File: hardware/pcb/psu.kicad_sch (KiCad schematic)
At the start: 24 parts, among them P1 2S LiPo Connector, Q3 AO3401A, SW1 SW_SPDT, U1 AP63203WU

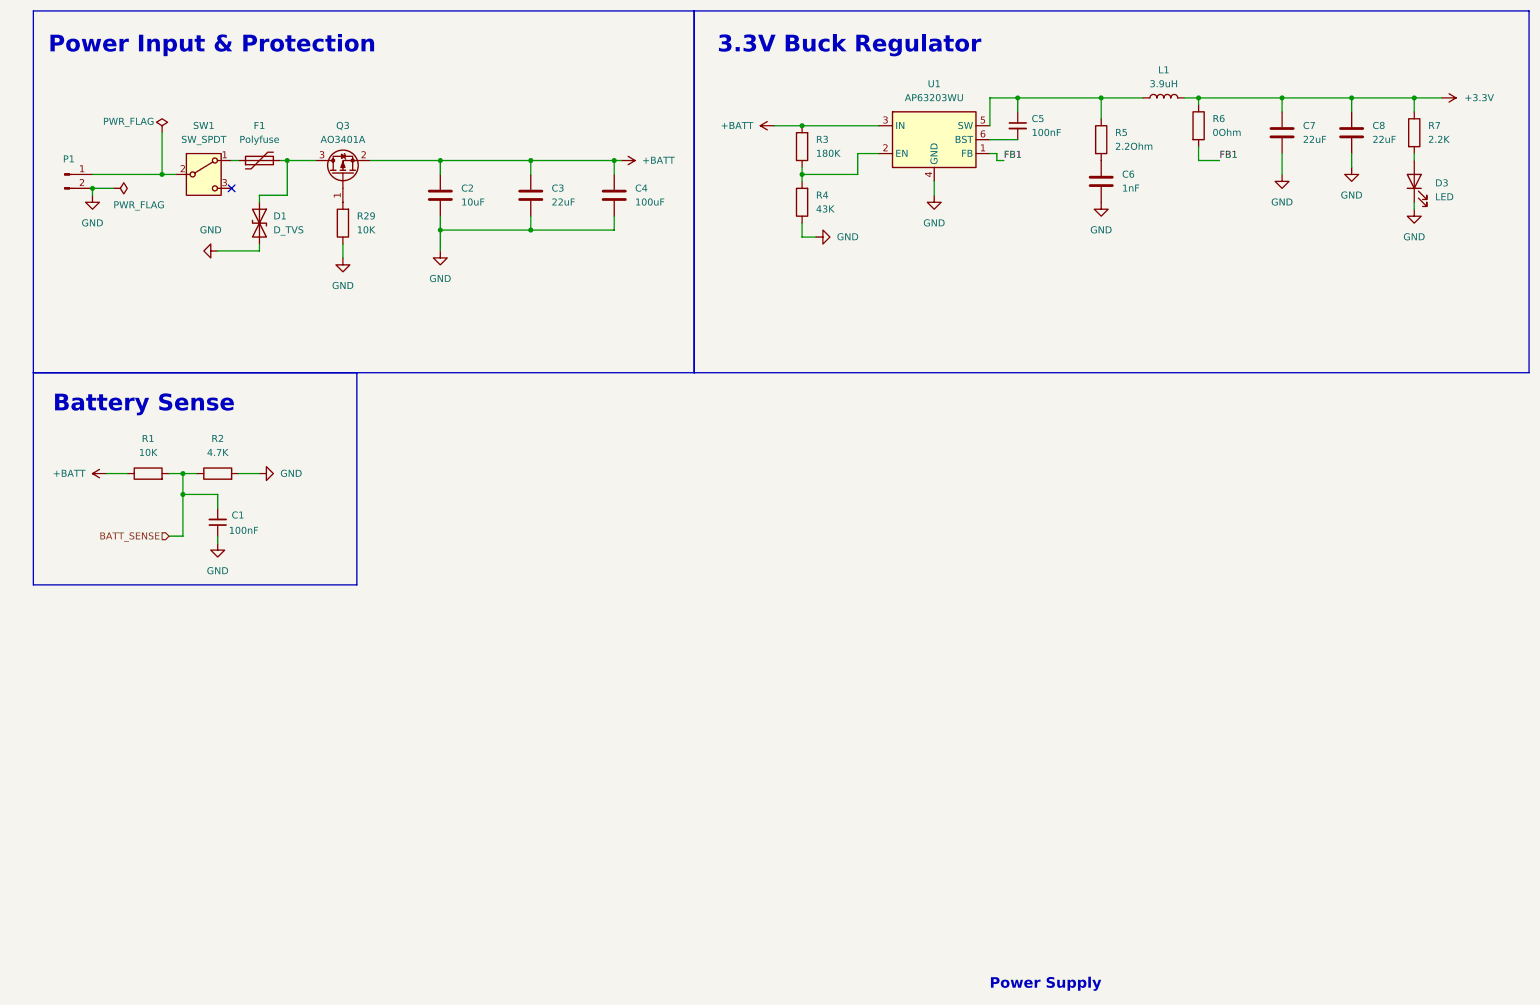
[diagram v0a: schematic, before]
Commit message: hardware: freeze schematic v1 after complete PCB redesign
Complete PCB and schematic refresh with reorganized sheets (psu, ui),
updated MCU/motor/sensor subsystems, and v1 schematic baseline frozen.
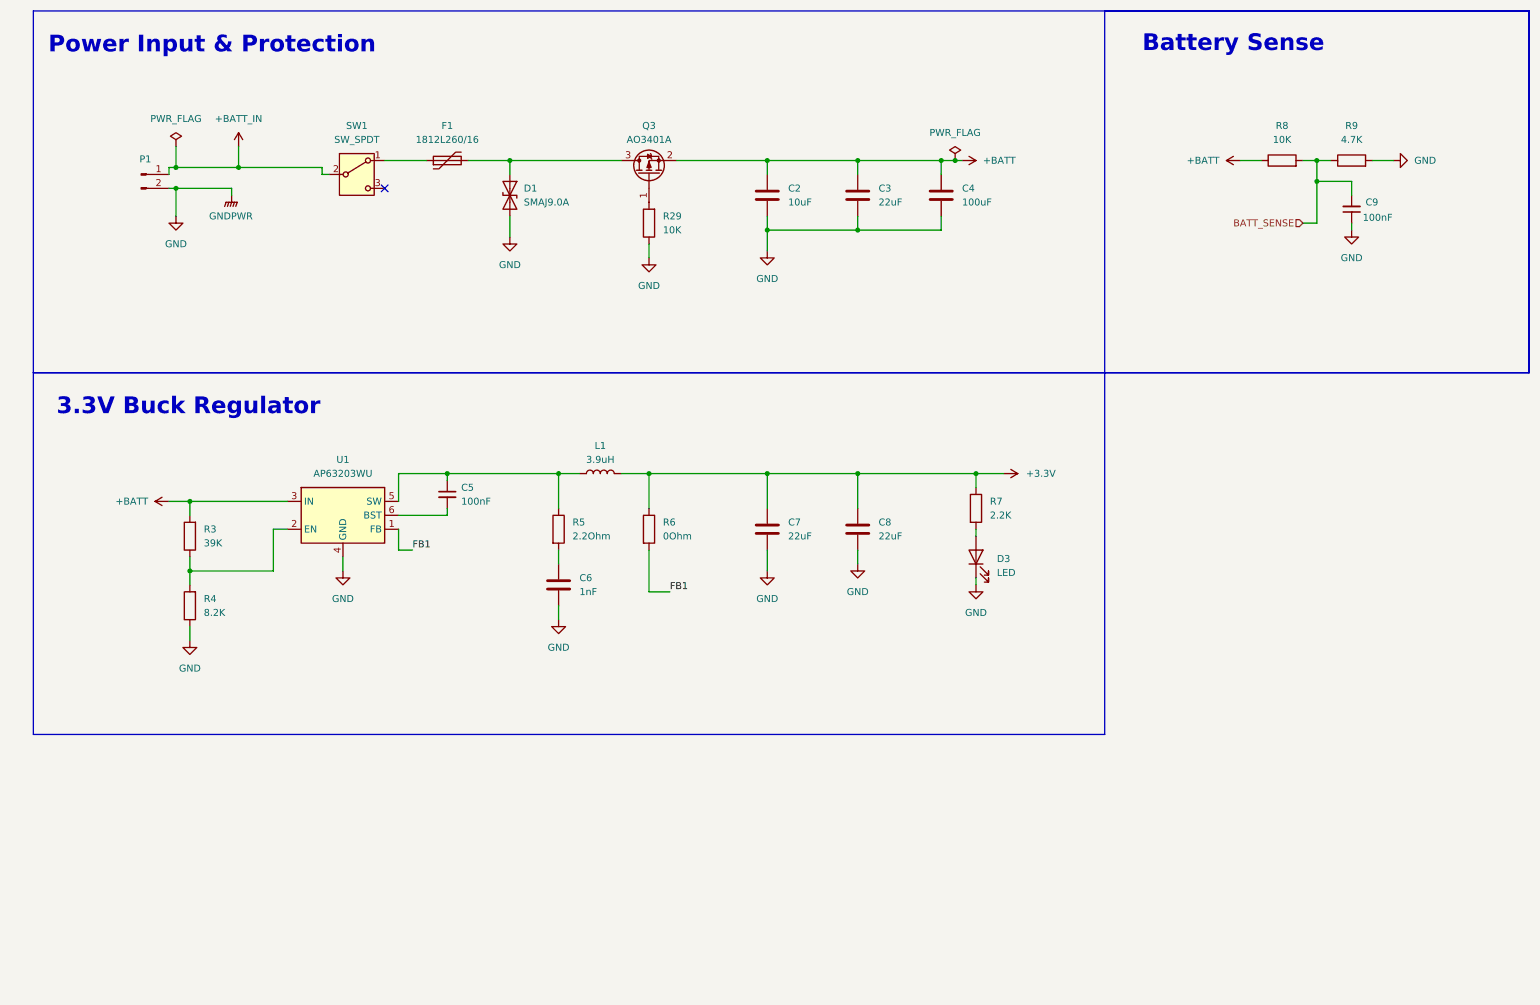
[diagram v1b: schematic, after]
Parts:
- removed C1: 100nF, Capacitor_SMD:C_0805_2012Metric_Pad1.18x1.45mm_HandSolder, symbol Device:C_Small
- removed R1: 10K, Resistor_SMD:R_0805_2012Metric_Pad1.20x1.40mm_HandSolder, symbol Device:R
- removed R2: 4.7K, Resistor_SMD:R_0805_2012Metric_Pad1.20x1.40mm_HandSolder, symbol Device:R
- added C9: 100nF, Capacitor_SMD:C_0805_2012Metric_Pad1.18x1.45mm_HandSolder, symbol Device:C_Small
- added R8: 10K, Resistor_SMD:R_0805_2012Metric_Pad1.20x1.40mm_HandSolder, symbol Device:R
- added R9: 4.7K, Resistor_SMD:R_0805_2012Metric_Pad1.20x1.40mm_HandSolder, symbol Device:R
- C2, C7, C8: footprint Capacitor_SMD:C_0603_1608Metric_Pad1.08x0.95mm_HandSolder -> Capacitor_SMD:C_1206_3216Metric_Pad1.33x1.80mm_HandSolder
- C3: footprint Capacitor_SMD:C_0805_2012Metric_Pad1.18x1.45mm_HandSolder -> Capacitor_SMD:C_1206_3216Metric_Pad1.33x1.80mm_HandSolder
- C4: footprint Capacitor_SMD:C_1210_3225Metric_Pad1.33x2.70mm_HandSolder -> Capacitor_SMD:C_1206_3216Metric_Pad1.33x1.80mm_HandSolder
- C6: footprint Capacitor_SMD:C_0805_2012Metric_Pad1.18x1.45mm_HandSolder -> Resistor_SMD:R_0805_2012Metric_Pad1.20x1.40mm_HandSolder
- D1: value D_TVS -> SMAJ9.0A
- F1: value Polyfuse -> 1812L260/16; footprint Fuse:Fuse_1206_3216Metric_Pad1.42x1.75mm_HandSolder -> Fuse:Fuse_1812_4532Metric
- L1: footprint Inductor_SMD:L_1210_3225Metric_Pad1.42x2.65mm_HandSolder -> Inductor_SMD:L_Sunlord_SWPA4030S
- R3: value 180K -> 39K
- R4: value 43K -> 8.2K
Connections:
- net +BATT: now also R8.1
- net BATT_SENSE: now also C9.2, R8.2, R9.1
- net GND: now also C9.1, R9.2
- net +BATT_IN: now reaches P1.1 (Pin_1), SW1.2 (B)
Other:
- note removed: "Power Supply"

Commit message: format öncesi commit
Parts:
- C2, C8: footprint Capacitor_SMD:C_1206_3216Metric_Pad1.33x1.80mm_HandSolder -> Capacitor_SMD:C_0805_2012Metric
- C3, C4: footprint Capacitor_SMD:C_1206_3216Metric_Pad1.33x1.80mm_HandSolder -> Capacitor_SMD:C_1206_3216Metric
- C5, C9: footprint Capacitor_SMD:C_0805_2012Metric_Pad1.18x1.45mm_HandSolder -> Capacitor_SMD:C_0603_1608Metric
- C6: footprint Resistor_SMD:R_0805_2012Metric_Pad1.20x1.40mm_HandSolder -> Capacitor_SMD:C_0603_1608Metric
- C7: footprint Capacitor_SMD:C_1206_3216Metric_Pad1.33x1.80mm_HandSolder -> Capacitor_SMD:C_0805_2012Metric_Pad1.18x1.45mm
- D3: footprint LED_SMD:LED_0805_2012Metric_Pad1.15x1.40mm_HandSolder -> LED_SMD:LED_0603_1608Metric
- R29, R3, R4, R7, R8, R9: footprint Resistor_SMD:R_0805_2012Metric_Pad1.20x1.40mm_HandSolder -> Resistor_SMD:R_0603_1608Metric
- R6: footprint Resistor_SMD:R_1206_3216Metric_Pad1.30x1.75mm_HandSolder -> Resistor_SMD:R_0603_1608Metric
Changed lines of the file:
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@@
 			)
 		)
-		(property "Footprint" "Capacitor_SMD:C_1206_3216Metric_Pad1.33x1.80mm_HandSolder"
+		(property "Footprint" "Capacitor_SMD:C_1206_3216Metric"
 			(at 163.5252 49.53 0)
 			(hide yes)
@@
 			)
 		)
-		(property "Footprint" "Capacitor_SMD:C_1206_3216Metric_Pad1.33x1.80mm_HandSolder"
+		(property "Footprint" "Capacitor_SMD:C_0805_2012Metric_Pad1.18x1.45mm"
 			(at 147.0152 110.49 0)
 			(hide yes)
@@
 			)
 		)
-		(property "Footprint" "Resistor_SMD:R_0805_2012Metric_Pad1.20x1.40mm_HandSolder"
+		(property "Footprint" "Resistor_SMD:R_0603_1608Metric"
 			(at 182.372 102.87 90)
 			(hide yes)
@@
 			)
 		)
-		(property "Footprint" "LED_SMD:LED_0805_2012Metric_Pad1.15x1.40mm_HandSolder"
+		(property "Footprint" "LED_SMD:LED_0603_1608Metric"
 			(at 184.15 111.76 0)
 			(hide yes)
@@
 			)
 		)
-		(property "Footprint" "Capacitor_SMD:C_0805_2012Metric_Pad1.18x1.45mm_HandSolder"
+		(property "Footprint" "Capacitor_SMD:C_0603_1608Metric"
 			(at 252.73 48.26 0)
 			(hide yes)
@@
 			)
 		)
-		(property "Footprint" "Resistor_SMD:R_0805_2012Metric_Pad1.20x1.40mm_HandSolder"
+		(property "Footprint" "Capacitor_SMD:C_0603_1608Metric"
 			(at 108.9152 120.65 0)
 			(hide yes)
@@
 			)
 		)
-		(property "Footprint" "Resistor_SMD:R_0805_2012Metric_Pad1.20x1.40mm_HandSolder"
+		(property "Footprint" "Resistor_SMD:R_0603_1608Metric"
 			(at 126.238 50.8 90)
 			(hide yes)
@@
 			)
 		)
-		(property "Footprint" "Resistor_SMD:R_0805_2012Metric_Pad1.20x1.40mm_HandSolder"
+		(property "Footprint" "Resistor_SMD:R_0603_1608Metric"
 			(at 42.418 107.95 90)
 			(hide yes)
@@
 			)
 		)
-		(property "Footprint" "Capacitor_SMD:C_0805_2012Metric_Pad1.18x1.45mm_HandSolder"
+		(property "Footprint" "Capacitor_SMD:C_0603_1608Metric"
 			(at 87.63 100.33 0)
 			(hide yes)
@@
 			)
 		)
-		(property "Footprint" "Resistor_SMD:R_0805_2012Metric_Pad1.20x1.40mm_HandSolder"
+		(property "Footprint" "Resistor_SMD:R_0603_1608Metric"
 			(at 42.418 120.65 90)
 			(hide yes)
@@
 			)
 		)
-		(property "Footprint" "Capacitor_SMD:C_1206_3216Metric_Pad1.33x1.80mm_HandSolder"
+		(property "Footprint" "Capacitor_SMD:C_1206_3216Metric"
 			(at 178.7652 49.53 0)
 			(hide yes)
@@
 			)
 		)
-		(property "Footprint" "Resistor_SMD:R_0805_2012Metric_Pad1.20x1.40mm_HandSolder"
+		(property "Footprint" "Resistor_SMD:R_0603_1608Metric"
 			(at 240.03 41.148 90)
 			(hide yes)
@@
 			)
 		)
-		(property "Footprint" "Resistor_SMD:R_1206_3216Metric_Pad1.30x1.75mm_HandSolder"
+		(property "Footprint" "Resistor_SMD:R_0603_1608Metric"
 			(at 122.682 106.68 90)
 			(hide yes)
@@
 			)
 		)
-		(property "Footprint" "Capacitor_SMD:C_1206_3216Metric_Pad1.33x1.80mm_HandSolder"
+		(property "Footprint" "Capacitor_SMD:C_0805_2012Metric"
 			(at 163.5252 110.49 0)
 			(hide yes)
@@
 			)
 		)
-		(property "Footprint" "Resistor_SMD:R_0805_2012Metric_Pad1.20x1.40mm_HandSolder"
+		(property "Footprint" "Resistor_SMD:R_0603_1608Metric"
 			(at 252.73 41.148 90)
 			(hide yes)
@@
 			)
 		)
-		(property "Footprint" "Capacitor_SMD:C_1206_3216Metric_Pad1.33x1.80mm_HandSolder"
+		(property "Footprint" "Capacitor_SMD:C_0805_2012Metric"
 			(at 147.0152 49.53 0)
 			(hide yes)
